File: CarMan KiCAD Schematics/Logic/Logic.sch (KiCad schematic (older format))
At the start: 40 parts, among them J1 MC_CAN, J3 IMU, J4 RTC, J5.1 Conn_01x08, J5.2 Conn_01x08, J6 You're Welcome -Ethan, J7 GLV BOB, J8 PIC program, U1 MCP9700AT-HTT, U10 TLP293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

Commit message: Aesthetics
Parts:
- removed J5.1, J5.2: Conn_01x08, symbol Connector_Generic:Conn_01x08
- added J5.1, J5.2: Conn_01x06, symbol Connector_Generic:Conn_01x06
- U6: symbol Lafayette_Electric_Car_Internals:RaspberryPi3 -> Logic-rescue:RaspberryPi3-Lafayette_Electric_Car_Internals
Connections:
- wire segments 250 -> 248
- no-connect marks 53 -> 51
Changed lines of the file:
@@
 5V_rtn
 $Comp
-L Lafayette_Electric_Car_Internals:RaspberryPi3 U?
+L Logic-rescue:RaspberryPi3-Lafayette_Electric_Car_Internals U?
 U 1 1 5F9FC061
 P 10000 4100
@@
 Text Label 7850 4500 2    50   ~ 0
 GLV_rtn
-Text Label 6000 7500 3    50   ~ 0
+Text Label 7400 5950 2    50   ~ 0
 CAN_H
-Text Label 6100 7500 3    50   ~ 0
+Text Label 7400 5850 2    50   ~ 0
 CAN_L
 $Comp
@@
 Wire Wire Line
 	7400 1550 7400 1250
-Text Label 5900 6100 1    50   ~ 0
-PC_ready
-Text Label 6000 6100 1    50   ~ 0
-Throttle_SEL
-Wire Wire Line
-	6000 5850 6000 6150
-Wire Wire Line
-	5900 5850 5900 6150
 Wire Wire Line
 	6550 5200 6350 5200
@@
 Wire Wire Line
 	10350 550  10350 900
-Text Label 6200 5850 1    50   ~ 0
-Safety_Loop
-Text Label 6300 5850 1    50   ~ 0
-5V_ISO_RTN
-Text Label 6500 5850 1    50   ~ 0
-SCL_TSI
-$Comp
-L power:PWR_FLAG #FLG0106
-U 1 1 5FB4B178
-P 6300 7250
-F 0 "#FLG0106" H 6300 7325 50  0001 C CNN
-F 1 "PWR_FLAG" H 6300 7423 50  0000 C CNN
-F 2 "" H 6300 7250 50  0001 C CNN
-F 3 "~" H 6300 7250 50  0001 C CNN
-	1    6300 7250
-	-1   0    0    1
-$EndComp
-Wire Wire Line
-	6300 6700 6300 7250
-Wire Wire Line
-	6500 6150 6500 5850
-Wire Wire Line
-	6400 6150 6400 5850
-Wire Wire Line
-	6300 6150 6300 5850
-Wire Wire Line
-	6200 6150 6200 5850
-Wire Wire Line
-	6100 6150 6100 5850
-Wire Wire Line
-	5900 7000 5900 6700
-Text Label 6400 5850 1    50   ~ 0
-SDA_TSI
-Text Label 6100 5850 1    50   ~ 0
-Cooling_CTRL
-Text Label 5900 6750 3    50   ~ 0
-RTDS_CTRL
-Text Label 6000 7200 3    50   ~ 0
+Text Label 6850 5950 0    50   ~ 0
 CAN+
-Text Label 6100 7200 3    50   ~ 0
+Text Label 6850 5850 0    50   ~ 0
 CAN-
-Wire Wire Line
-	6200 6700 6200 7000
-Text Label 6200 6750 3    50   ~ 0
-SR_CTRL
-Text Label 6300 6750 3    50   ~ 0
-5V_non_iso
 NoConn ~ 2700 3300
-NoConn ~ 5800 6150
 NoConn ~ 2700 3400
 NoConn ~ 2700 3500
@@
 NoConn ~ 6350 3600
 NoConn ~ 6350 3700
-$Comp
-L Connector_Generic:Conn_01x08 J5.1
-U 1 1 5FCBCDE5
-P 6200 6350
-F 0 "J5.1" V 6118 6730 50  0000 L CNN
-F 1 "Conn_01x08" V 6163 6730 50  0001 L CNN
-F 2 "" H 6200 6350 50  0001 C CNN
-F 3 "~" H 6200 6350 50  0001 C CNN
-	1    6200 6350
-	0    1    1    0
-$EndComp
-$Comp
-L Connector_Generic:Conn_01x08 J5.2
-U 1 1 5FCE2C74
-P 6200 6500
-F 0 "J5.2" V 6118 6880 50  0000 L CNN
-F 1 "Conn_01x08" V 6163 6880 50  0001 L CNN
-F 2 "" H 6200 6500 50  0001 C CNN
-F 3 "~" H 6200 6500 50  0001 C CNN
-	1    6200 6500
-	0    1    -1   0
-$EndComp
-NoConn ~ 5800 6700
-Wire Wire Line
-	6100 6700 6100 7750
-Wire Wire Line
-	6000 6700 6000 7750
-Text Label 6100 6750 3    50   ~ 0
-BP_CAN-
-Text Label 6000 6750 3    50   ~ 0
-BP_CAN+
-Wire Wire Line
-	6500 6700 6500 7000
-Wire Wire Line
-	6400 6700 6400 7000
-Text Label 6500 7000 3    50   ~ 0
-AMS_Fault
-Text Label 6400 7000 3    50   ~ 0
-GLV_rtn
 Text Label 10950 1700 0    50   ~ 0
 GLV_rtn
@@
 Wire Wire Line
 	10450 850  10450 900
+Text Label 6750 6050 2    50   ~ 0
+RTDS_CTRL
+Wire Wire Line
+	6350 5850 7400 5850
+Wire Wire Line
+	6350 5950 7400 5950
+Text Label 6400 5850 0    50   ~ 0
+BP_CAN-
+Text Label 6400 5950 0    50   ~ 0
+BP_CAN+
+$Comp
+L Connector_Generic:Conn_01x06 J5.2
+U 1 1 5FB98586
+P 6150 5850
+F 0 "J5.2" H 6050 6150 50  0000 L CNN
+F 1 "Conn_01x06" H 6230 5751 50  0001 L CNN
+F 2 "" H 6150 5850 50  0001 C CNN
+F 3 "~" H 6150 5850 50  0001 C CNN
+	1    6150 5850
+	-1   0    0    -1
+$EndComp
+$Comp
+L Connector_Generic:Conn_01x06 J5.1
+U 1 1 5FB8432E
+P 5950 5850
+F 0 "J5.1" H 5850 6150 50  0000 L CNN
+F 1 "Conn_01x06" H 6030 5751 50  0001 L CNN
+F 2 "" H 5950 5850 50  0001 C CNN
+F 3 "~" H 5950 5850 50  0001 C CNN
+	1    5950 5850
+	1    0    0    -1
+$EndComp
+Text Label 6750 6150 2    50   ~ 0
+PC_ready
+Text Label 5300 6150 0    50   ~ 0
+Throttle_SEL
+Text Label 5300 5950 0    50   ~ 0
+Safety_Loop
+Text Label 5300 5850 0    50   ~ 0
+5V_ISO_RTN
+Text Label 5300 5650 0    50   ~ 0
+SCL_TSI
+Text Label 5300 5750 0    50   ~ 0
+SDA_TSI
+Text Label 5300 6050 0    50   ~ 0
+Cooling_CTRL
+Text Label 6750 5650 2    50   ~ 0
+AMS_Fault
+Text Label 6750 5750 2    50   ~ 0
+SR_CTRL
+Wire Wire Line
+	6350 6150 6750 6150
+Wire Wire Line
+	6350 5650 6750 5650
+Wire Wire Line
+	6350 5750 6750 5750
+Wire Wire Line
+	6350 6050 6750 6050
+Wire Wire Line
+	5300 6150 5750 6150
+Wire Wire Line
+	5300 6050 5750 6050
+Wire Wire Line
+	5300 5950 5750 5950
+Wire Wire Line
+	5300 5850 5750 5850
+Wire Wire Line
+	5300 5750 5750 5750
+Wire Wire Line
+	5300 5650 5750 5650
 $EndSCHEMATC

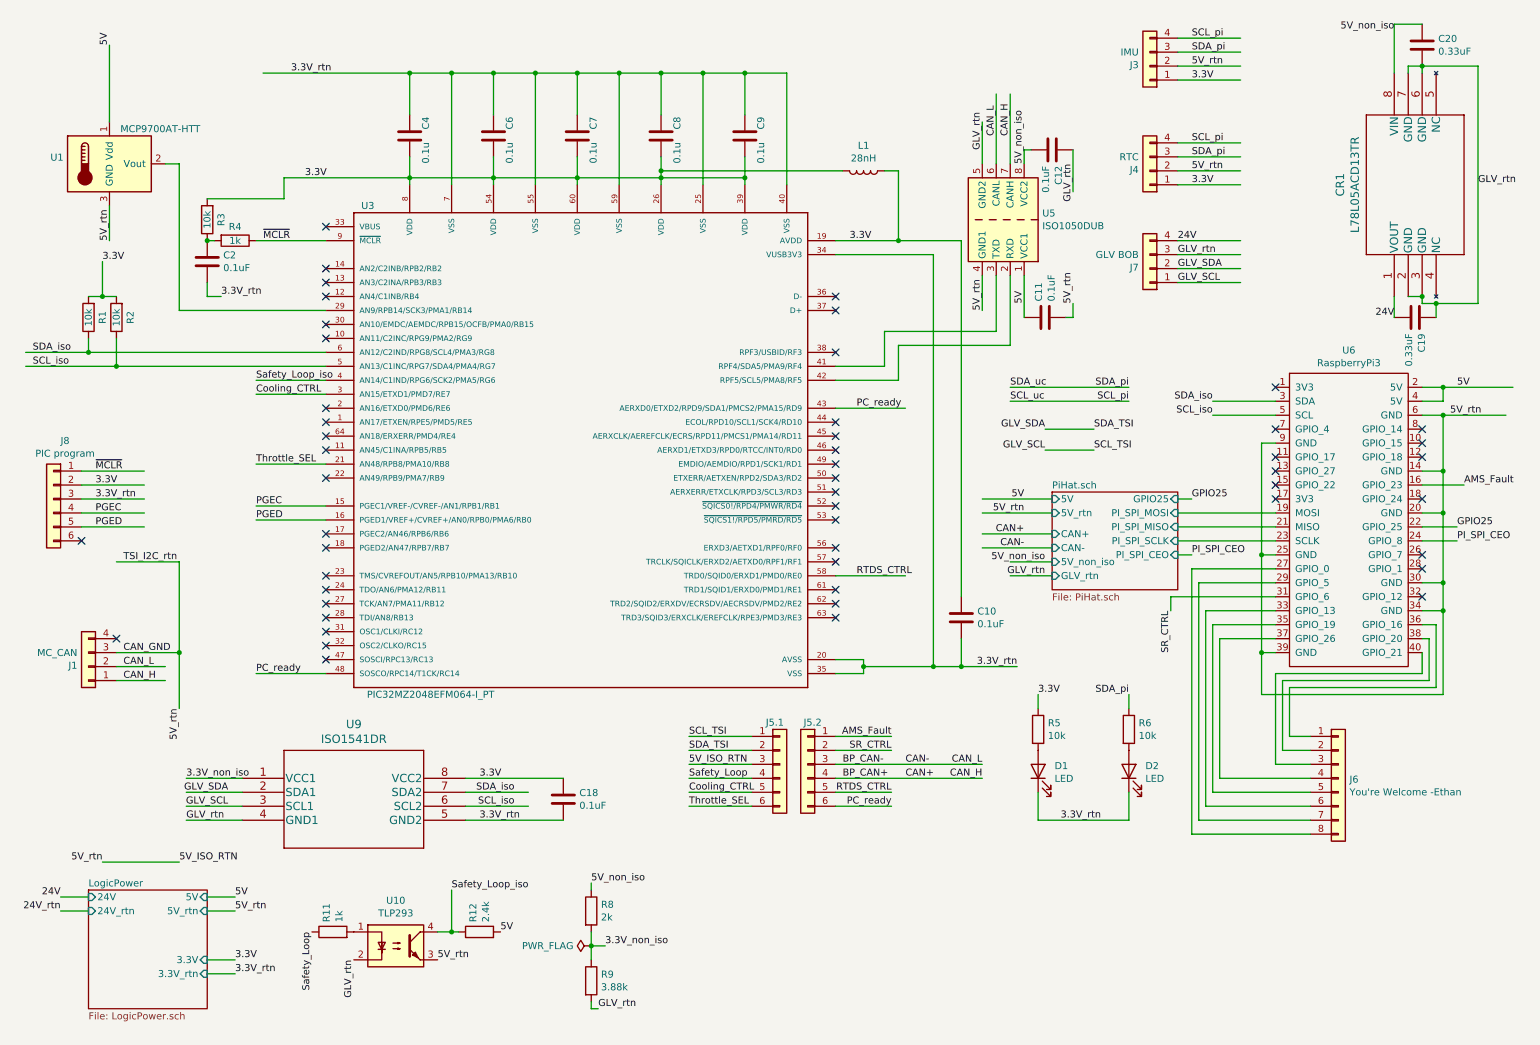
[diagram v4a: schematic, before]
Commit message: Logic Footprints in General Library, Added Logic LEDs
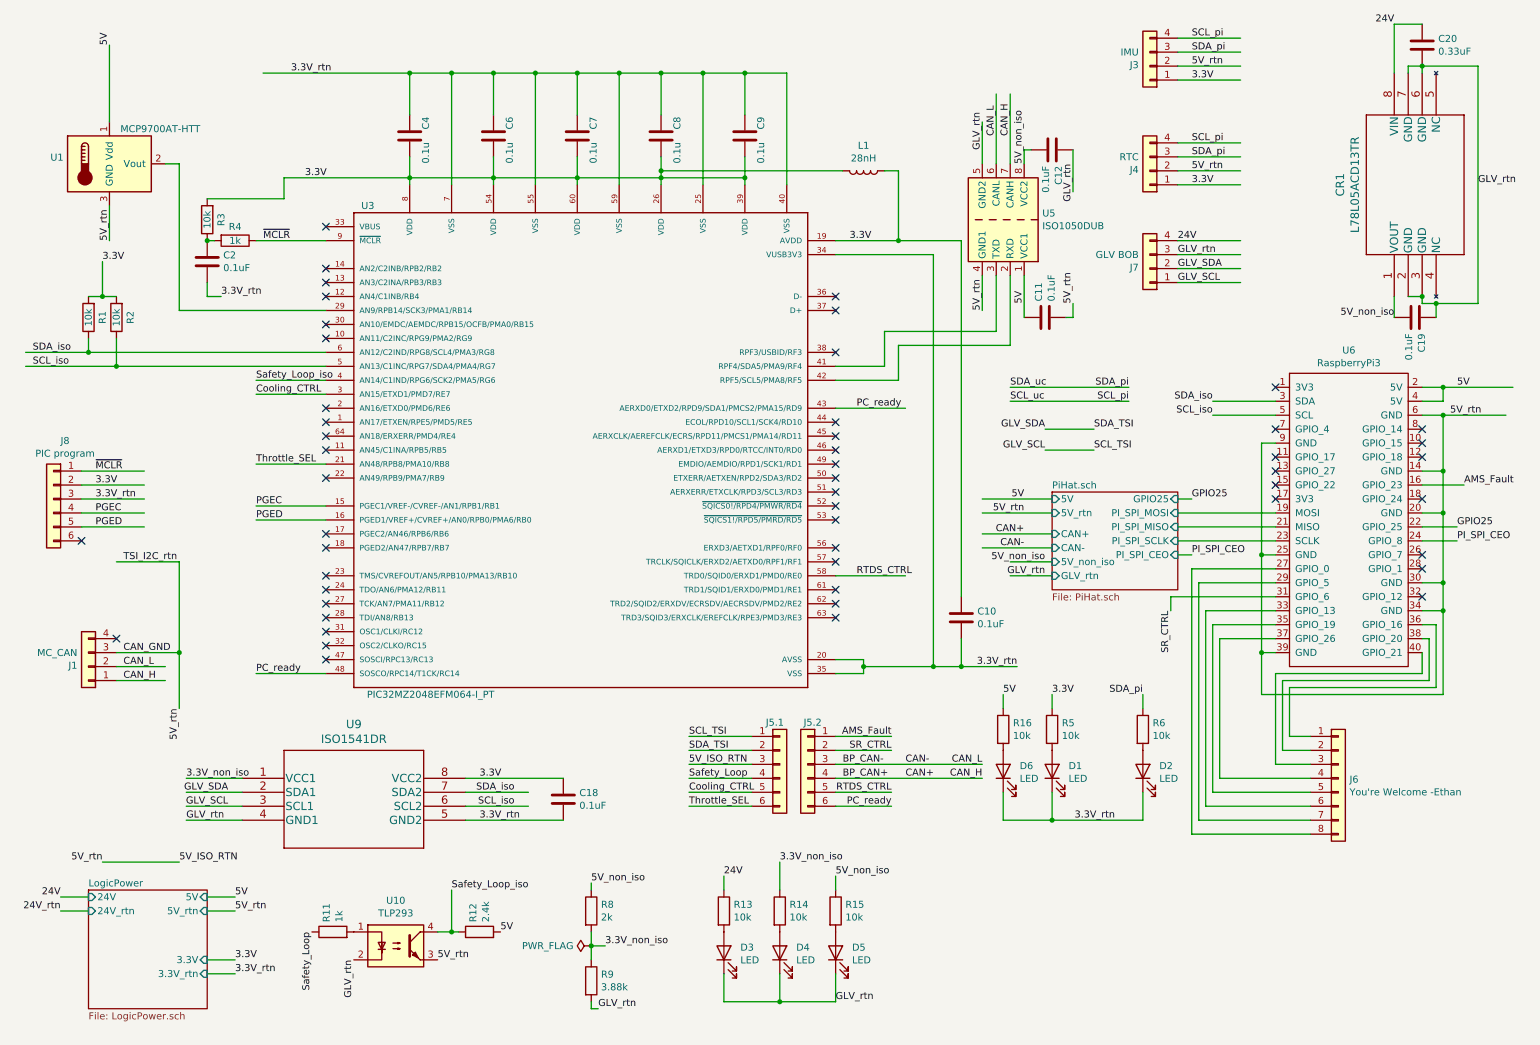
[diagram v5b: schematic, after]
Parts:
- added D3, D4, D5, D6: LED, CarMan General Footprints:VAOL-S8GT4, symbol Device:LED
- added R13, R14, R15, R16: 10k, Resistor_SMD:R_0815_2038Metric_Pad1.53x4.00mm_HandSolder, symbol Device:R
- C10, C11, C12, C18, C2, C20, C4, C6, C7, C8, C9: footprint (none) -> Capacitor_SMD:C_0805_2012Metric_Pad1.15x1.40mm_HandSolder
- C19: value 0.33uF -> 0.1uF; footprint (none) -> Capacitor_SMD:C_0805_2012Metric_Pad1.15x1.40mm_HandSolder
- CR1: footprint SO-8_STM -> CarMan General Footprints:L78L05ACD13TR
- D1, D2: footprint (none) -> CarMan General Footprints:VAOL-S8GT4
- J1, J7: footprint (none) -> CarMan General Footprints:Molex_MiniFit-JR-5556-04A_2x02x4.20mm_Straight
- L1: footprint (none) -> Inductor_SMD:L_0805_2012Metric_Pad1.15x1.40mm_HandSolder
- R1, R11, R12, R2, R3, R4, R5, R6, R8, R9: footprint (none) -> Resistor_SMD:R_0815_2038Metric_Pad1.53x4.00mm_HandSolder
- U3: footprint QFP50P1200X1200X120-64N -> CarMan General Footprints:QFP50P1200X1200X120-64N
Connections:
- wire segments 248 -> 259
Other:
- moved on the sheet: D1, D2, R5, R6

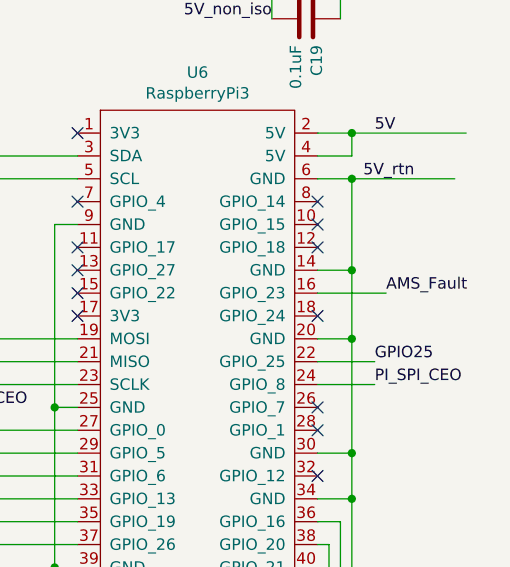
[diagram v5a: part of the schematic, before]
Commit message: Added AIRS monitor signal to Pi, added all Logic Footprints
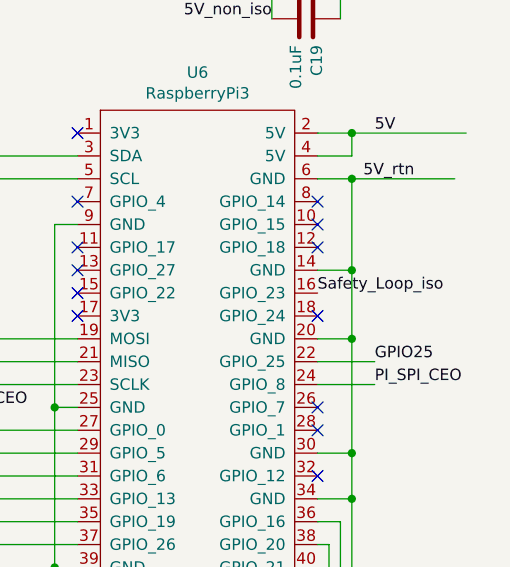
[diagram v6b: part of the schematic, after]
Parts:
- J3, J4: footprint (none) -> Connector_PinSocket_2.54mm:PinSocket_1x04_P2.54mm_Horizontal
- J5.1, J5.2, J8: footprint (none) -> Connector_PinSocket_2.54mm:PinSocket_1x06_P2.54mm_Vertical
- J6: footprint (none) -> Connector_PinSocket_2.54mm:PinSocket_1x08_P2.54mm_Vertical
- U6: footprint Lafayette_Electric_Car_Footprints:RaspberryPi3 -> CarMan General Footprints:Raspberry_Pi_3_B
- U9: footprint D8_TEX -> CarMan General Footprints:ISO1541DR
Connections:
- wire segments 259 -> 258
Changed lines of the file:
@@
 F 0 "J3" H 8680 842 50  0000 L CNN
 F 1 "IMU" H 8680 751 50  0000 L CNN
-F 2 "" H 8600 850 50  0001 C CNN
+F 2 "Connector_PinSocket_2.54mm:PinSocket_1x04_P2.54mm_Horizontal" H 8600 850 50  0001 C CNN
 F 3 "~" H 8600 850 50  0001 C CNN
 	1    8600 850
@@
 F 0 "J4" H 8680 1592 50  0000 L CNN
 F 1 "RTC" H 8680 1501 50  0000 L CNN
-F 2 "" H 8600 1600 50  0001 C CNN
+F 2 "Connector_PinSocket_2.54mm:PinSocket_1x04_P2.54mm_Horizontal" H 8600 1600 50  0001 C CNN
 F 3 "~" H 8600 1600 50  0001 C CNN
 	1    8600 1600
@@
 F 0 "U6" H 10025 5315 50  0000 C CNN
 F 1 "RaspberryPi3" H 10025 5224 50  0000 C CNN
-F 2 "Lafayette_Electric_Car_Footprints:RaspberryPi3" H 10250 5300 50  0001 C CNN
+F 2 "CarMan General Footprints:Raspberry_Pi_3_B" H 10250 5300 50  0001 C CNN
 F 3 "" H 10250 5300 50  0001 C CNN
 	1    10000 4100
@@
 F 0 "J6" H 10030 5942 50  0000 L CNN
 F 1 "You're Welcome -Ethan" H 10030 5851 50  0000 L CNN
-F 2 "" H 9950 5950 50  0001 C CNN
+F 2 "Connector_PinSocket_2.54mm:PinSocket_1x08_P2.54mm_Vertical" H 9950 5950 50  0001 C CNN
 F 3 "~" H 9950 5950 50  0001 C CNN
 	1    9950 5950
@@
 F 0 "J8" H 668 4367 50  0000 C CNN
 F 1 "PIC program" H 668 4276 50  0000 C CNN
-F 2 "" H 750 3950 50  0001 C CNN
+F 2 "Connector_PinSocket_2.54mm:PinSocket_1x06_P2.54mm_Vertical" H 750 3950 50  0001 C CNN
 F 3 "~" H 750 3950 50  0001 C CNN
 	1    750  3950
@@
 Wire Wire Line
 	8800 2400 9250 2400
-Wire Wire Line
-	10550 3850 10850 3850
-Text Label 10850 3850 0    50   ~ 0
-AMS_Fault
 Text Label 7850 3450 2    50   ~ 0
 GLV_SDA
@@
 F 0 "U9" H 2900 6337 60  0000 C CNN
 F 1 "ISO1541DR" H 2900 6231 60  0000 C CNN
-F 2 "D8_TEX" H 2900 6190 60  0001 C CNN
-F 3 "" H 2100 5950 60  0000 C CNN
+F 2 "CarMan General Footprints:ISO1541DR" H 2900 6190 60  0001 C CNN
+F 3 "https://www.ti.com/lit/ds/symlink/iso1541.pdf?HQS=TI-null-null-digikeymode-df-pf-null-wwe&ts=1606082283174" H 2100 5950 60  0001 C CNN
 	1    2100 5950
 	1    0    0    -1
@@
 F 0 "J5.2" H 6050 6150 50  0000 L CNN
 F 1 "Conn_01x06" H 6230 5751 50  0001 L CNN
-F 2 "" H 6150 5850 50  0001 C CNN
+F 2 "Connector_PinSocket_2.54mm:PinSocket_1x06_P2.54mm_Vertical" H 6150 5850 50  0001 C CNN
 F 3 "~" H 6150 5850 50  0001 C CNN
 	1    6150 5850
@@
 F 0 "J5.1" H 5850 6150 50  0000 L CNN
 F 1 "Conn_01x06" H 6030 5751 50  0001 L CNN
-F 2 "" H 5950 5850 50  0001 C CNN
+F 2 "Connector_PinSocket_2.54mm:PinSocket_1x06_P2.54mm_Vertical" H 5950 5850 50  0001 C CNN
 F 3 "~" H 5950 5850 50  0001 C CNN
 	1    5950 5850
@@
 Wire Wire Line
 	7900 6250 8550 6250
+Text Label 10550 3850 0    50   ~ 0
+Safety_Loop_iso
 $EndSCHEMATC

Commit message: Logic PCB started, Pi 3B footprint fixed
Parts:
- J3, J4: footprint Connector_PinSocket_2.54mm:PinSocket_1x04_P2.54mm_Horizontal -> Connector_PinHeader_2.54mm:PinHeader_1x04_P2.54mm_Vertical
- R1, R11, R12, R13, R14, R15, R16, R2, R3, R4, R5, R6, R8, R9: footprint Resistor_SMD:R_0815_2038Metric_Pad1.53x4.00mm_HandSolder -> Resistor_SMD:R_0805_2012Metric_Pad1.15x1.40mm_HandSolder
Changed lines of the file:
@@
 F 0 "J3" H 8680 842 50  0000 L CNN
 F 1 "IMU" H 8680 751 50  0000 L CNN
-F 2 "Connector_PinSocket_2.54mm:PinSocket_1x04_P2.54mm_Horizontal" H 8600 850 50  0001 C CNN
+F 2 "Connector_PinHeader_2.54mm:PinHeader_1x04_P2.54mm_Vertical" H 8600 850 50  0001 C CNN
 F 3 "~" H 8600 850 50  0001 C CNN
 	1    8600 850
@@
 F 0 "J4" H 8680 1592 50  0000 L CNN
 F 1 "RTC" H 8680 1501 50  0000 L CNN
-F 2 "Connector_PinSocket_2.54mm:PinSocket_1x04_P2.54mm_Horizontal" H 8600 1600 50  0001 C CNN
+F 2 "Connector_PinHeader_2.54mm:PinHeader_1x04_P2.54mm_Vertical" H 8600 1600 50  0001 C CNN
 F 3 "~" H 8600 1600 50  0001 C CNN
 	1    8600 1600
@@
 F 0 "R2" V 1100 2650 50  0000 C CNN
 F 1 "10k" V 1200 2650 50  0000 C CNN
-F 2 "Resistor_SMD:R_0815_2038Metric_Pad1.53x4.00mm_HandSolder" V 1130 2650 50  0001 C CNN
+F 2 "Resistor_SMD:R_0805_2012Metric_Pad1.15x1.40mm_HandSolder" V 1130 2650 50  0001 C CNN
 F 3 "~" H 1200 2650 50  0001 C CNN
 	1    1200 2650
@@
 F 0 "R1" V 900 2650 50  0000 C CNN
 F 1 "10k" V 1000 2650 50  0000 C CNN
-F 2 "Resistor_SMD:R_0815_2038Metric_Pad1.53x4.00mm_HandSolder" V 930 2650 50  0001 C CNN
+F 2 "Resistor_SMD:R_0805_2012Metric_Pad1.15x1.40mm_HandSolder" V 930 2650 50  0001 C CNN
 F 3 "~" H 1000 2650 50  0001 C CNN
 	1    1000 2650
@@
 F 0 "R3" V 1750 1950 50  0000 C CNN
 F 1 "10k" V 1850 1950 50  0000 C CNN
-F 2 "Resistor_SMD:R_0815_2038Metric_Pad1.53x4.00mm_HandSolder" V 1780 1950 50  0001 C CNN
+F 2 "Resistor_SMD:R_0805_2012Metric_Pad1.15x1.40mm_HandSolder" V 1780 1950 50  0001 C CNN
 F 3 "~" H 1850 1950 50  0001 C CNN
 	1    1850 1950
@@
 F 0 "R4" V 1950 2100 50  0000 C CNN
 F 1 "1k" V 2050 2100 50  0000 C CNN
-F 2 "Resistor_SMD:R_0815_2038Metric_Pad1.53x4.00mm_HandSolder" V 1980 2100 50  0001 C CNN
+F 2 "Resistor_SMD:R_0805_2012Metric_Pad1.15x1.40mm_HandSolder" V 1980 2100 50  0001 C CNN
 F 3 "~" H 2050 2100 50  0001 C CNN
 	1    2050 2100
@@
 F 0 "R5" H 7970 5646 50  0000 L CNN
 F 1 "10k" H 7970 5555 50  0000 L CNN
-F 2 "Resistor_SMD:R_0815_2038Metric_Pad1.53x4.00mm_HandSolder" V 7830 5600 50  0001 C CNN
+F 2 "Resistor_SMD:R_0805_2012Metric_Pad1.15x1.40mm_HandSolder" V 7830 5600 50  0001 C CNN
 F 3 "~" H 7900 5600 50  0001 C CNN
 	1    7900 5600
@@
 F 0 "R6" H 8620 5646 50  0000 L CNN
 F 1 "10k" H 8620 5555 50  0000 L CNN
-F 2 "Resistor_SMD:R_0815_2038Metric_Pad1.53x4.00mm_HandSolder" V 8480 5600 50  0001 C CNN
+F 2 "Resistor_SMD:R_0805_2012Metric_Pad1.15x1.40mm_HandSolder" V 8480 5600 50  0001 C CNN
 F 3 "~" H 8550 5600 50  0001 C CNN
 	1    8550 5600
@@
 F 0 "R8" H 4670 6946 50  0000 L CNN
 F 1 "2k" H 4670 6855 50  0000 L CNN
-F 2 "Resistor_SMD:R_0815_2038Metric_Pad1.53x4.00mm_HandSolder" V 4530 6900 50  0001 C CNN
+F 2 "Resistor_SMD:R_0805_2012Metric_Pad1.15x1.40mm_HandSolder" V 4530 6900 50  0001 C CNN
 F 3 "~" H 4600 6900 50  0001 C CNN
 	1    4600 6900
@@
 F 0 "R9" H 4670 7446 50  0000 L CNN
 F 1 "3.88k" H 4670 7355 50  0000 L CNN
-F 2 "Resistor_SMD:R_0815_2038Metric_Pad1.53x4.00mm_HandSolder" V 4530 7400 50  0001 C CNN
+F 2 "Resistor_SMD:R_0805_2012Metric_Pad1.15x1.40mm_HandSolder" V 4530 7400 50  0001 C CNN
 F 3 "~" H 4600 7400 50  0001 C CNN
 	1    4600 7400
@@
 F 0 "R12" H 3870 7096 50  0000 L CNN
 F 1 "2.4k" H 3870 7005 50  0000 L CNN
-F 2 "Resistor_SMD:R_0815_2038Metric_Pad1.53x4.00mm_HandSolder" V 3730 7050 50  0001 C CNN
+F 2 "Resistor_SMD:R_0805_2012Metric_Pad1.15x1.40mm_HandSolder" V 3730 7050 50  0001 C CNN
 F 3 "~" H 3800 7050 50  0001 C CNN
 	1    3800 7050
@@
 F 0 "R11" H 2820 7096 50  0000 L CNN
 F 1 "1k" H 2820 7005 50  0000 L CNN
-F 2 "Resistor_SMD:R_0815_2038Metric_Pad1.53x4.00mm_HandSolder" V 2680 7050 50  0001 C CNN
+F 2 "Resistor_SMD:R_0805_2012Metric_Pad1.15x1.40mm_HandSolder" V 2680 7050 50  0001 C CNN
 F 3 "~" H 2750 7050 50  0001 C CNN
 	1    2750 7050
@@
 F 0 "R15" H 6420 6946 50  0000 L CNN
 F 1 "10k" H 6420 6855 50  0000 L CNN
-F 2 "Resistor_SMD:R_0815_2038Metric_Pad1.53x4.00mm_HandSolder" V 6280 6900 50  0001 C CNN
+F 2 "Resistor_SMD:R_0805_2012Metric_Pad1.15x1.40mm_HandSolder" V 6280 6900 50  0001 C CNN
 F 3 "~" H 6350 6900 50  0001 C CNN
 	1    6350 6900
@@
 F 0 "R13" H 5620 6946 50  0000 L CNN
 F 1 "10k" H 5620 6855 50  0000 L CNN
-F 2 "Resistor_SMD:R_0815_2038Metric_Pad1.53x4.00mm_HandSolder" V 5480 6900 50  0001 C CNN
+F 2 "Resistor_SMD:R_0805_2012Metric_Pad1.15x1.40mm_HandSolder" V 5480 6900 50  0001 C CNN
 F 3 "~" H 5550 6900 50  0001 C CNN
 	1    5550 6900
@@
 F 0 "R14" H 6020 6946 50  0000 L CNN
 F 1 "10k" H 6020 6855 50  0000 L CNN
-F 2 "Resistor_SMD:R_0815_2038Metric_Pad1.53x4.00mm_HandSolder" V 5880 6900 50  0001 C CNN
+F 2 "Resistor_SMD:R_0805_2012Metric_Pad1.15x1.40mm_HandSolder" V 5880 6900 50  0001 C CNN
 F 3 "~" H 5950 6900 50  0001 C CNN
 	1    5950 6900
@@
 F 0 "R16" H 7620 5646 50  0000 L CNN
 F 1 "10k" H 7620 5555 50  0000 L CNN
-F 2 "Resistor_SMD:R_0815_2038Metric_Pad1.53x4.00mm_HandSolder" V 7480 5600 50  0001 C CNN
+F 2 "Resistor_SMD:R_0805_2012Metric_Pad1.15x1.40mm_HandSolder" V 7480 5600 50  0001 C CNN
 F 3 "~" H 7550 5600 50  0001 C CNN
 	1    7550 5600
